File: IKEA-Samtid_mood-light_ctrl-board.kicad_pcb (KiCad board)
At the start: 2 copper layers, 41.3 x 15.5 mm, 15 parts, among them IC1 ATMEGA168PA-M, P1 FTDI, P3.2 B-to-B-1B, P4.2 B-to-B-2B, SW1 ENTER, SW2 MODE, X1 CSTCE16M0V53-R0

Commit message: Being creative...
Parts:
- added DS1: DIODESCH, my_parts:MADW__diode_sub-SMA, F.Cu at (135.1, 95.6)
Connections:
- C1 pad 1: /VCC.B -> /VCC.B2
- IC1 pad 18: /VCC.B -> /VCC.B2
- IC1 pad 30: /RXI -> /RXI.B
- IC1 pad 31: /TXO -> /TXO.B
- IC1 pad 4: /VCC.B -> /VCC.B2
- IC1 pad 6: /VCC.B -> /VCC.B2
- IC1 pad 9: (no net) -> /LEDS.B
- JP1 pad 2: /VCC.B -> /VCC.B2
- P1 pad 3: /VCC.B -> /VCC.B2
- P1 pad 4: /RXI -> /RXI.B
- P1 pad 5: /TXO -> /TXO.B
- P3.2 pad 1: /TXO -> /LEDS.B
- P4.2 pad 1: (no net) -> /RXI.B
- P4.2 pad 3: (no net) -> /TXO.B
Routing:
- net /VCC.B2: track 0.00 -> 40.1 mm, vias 0 -> 3
- net /VCC.B: track 34.8 -> 4.26 mm, vias 3 -> 0
- net /TXO: track 19.4 -> 0.00 mm
- net /TXO.B: track 0.00 -> 18.6 mm
- net /RXI.B: track 0.00 -> 15.8 mm, vias 0 -> 1
- net /LEDS.B: track 0.00 -> 9.26 mm, vias 0 -> 1
- net /RXI: track 4.51 -> 0.00 mm, vias 1 -> 0
- net /MOSI: track 23.1 -> 24.7 mm
- net /XTAL1: track 5.93 -> 6.52 mm
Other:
- board text added: "mood-l. ctrl V0.40.a"
- board text removed: "mood-l. ctrl V0.31.b"

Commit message: 180-d the microMaTch connectors to prevent plugging in old boards.
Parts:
- DS1: value DIODESCH -> SS14L
- turned P3.2 to 116 degrees
- turned P4.2 to 64 degrees
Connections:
- P3.2 pad 1: /LEDS.B -> /GND.B
- P3.2 pad 2: /VCC.B -> /GND.B
- P3.2 pad 3: /GND.B -> /VCC.B
- P3.2 pad 4: /GND.B -> /LEDS.B
- P4.2 pad 1: /RXI.B -> /TXO.B
- P4.2 pad 3: /TXO.B -> /RXI.B
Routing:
- net /TXO.B: track 18.6 -> 17.4 mm
- net /RXI.B: track 15.8 -> 16.8 mm

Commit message: Playing with HC-05 placement.
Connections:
- C2 pad 2: /DTR -> /DTR.B
- P1 pad 6: /DTR -> /DTR.B
- P3.2 pad 2: /GND.B -> /DTR.B
- R2 pad 2: /DTR -> /DTR.B
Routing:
- net /DTR.B: track 0.00 -> 27.9 mm, vias 0 -> 6
- net /DTR: track 6.57 -> 0.00 mm
- net /RXI.B: track 16.8 -> 18.2 mm
- net /ADC2: track 9.76 -> 10.3 mm
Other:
- board text added: "3V!"
- board text removed: "5V!"

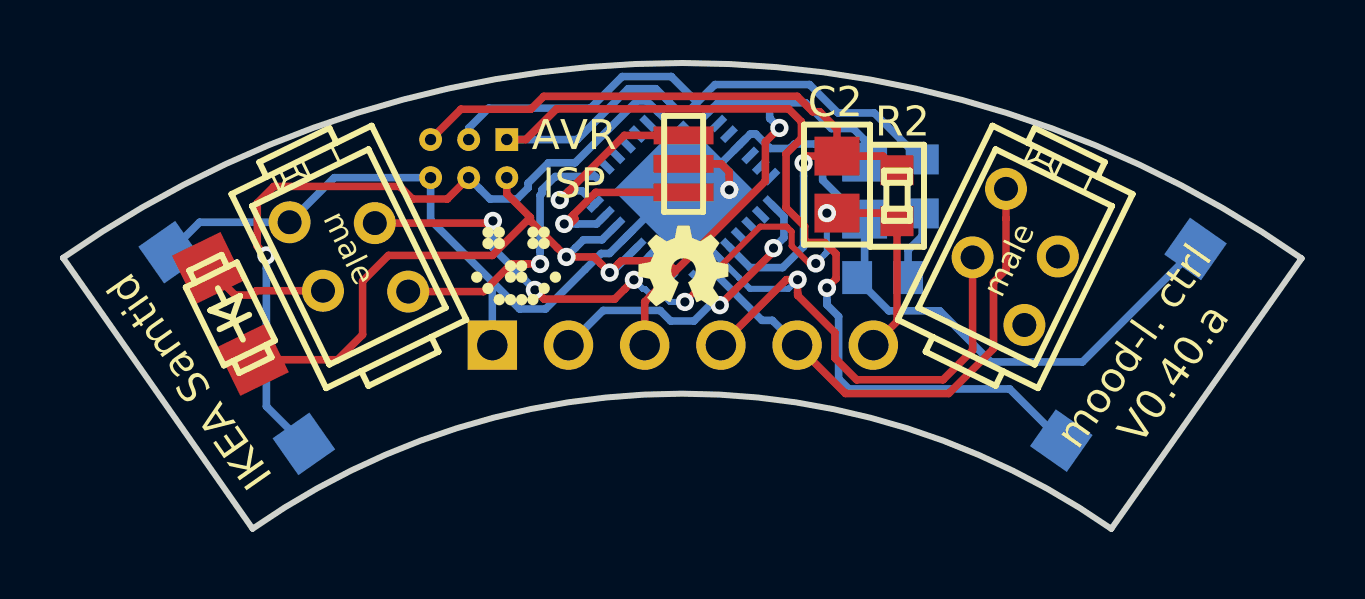
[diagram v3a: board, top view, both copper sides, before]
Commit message: HC-05 tweaks. Forgot about on-board 3.3V regulator.
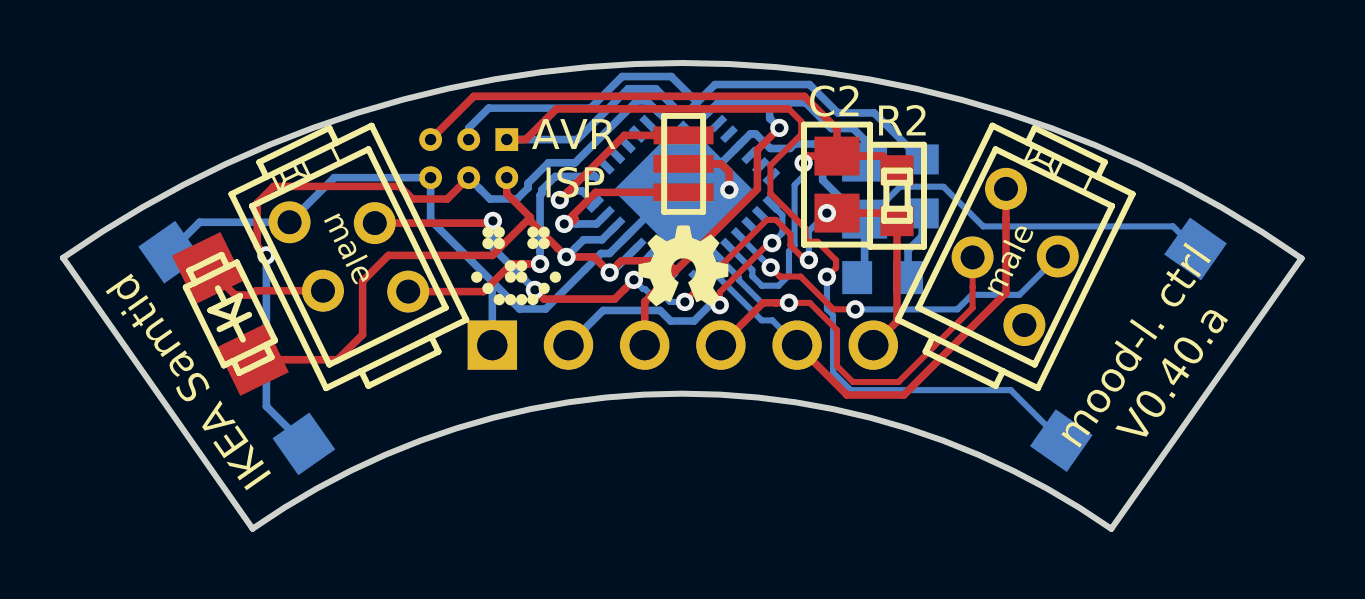
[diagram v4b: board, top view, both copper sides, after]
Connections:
- IC1 pad 28: (no net) -> /KEY.B
- P4.2 pad 2: (no net) -> /KEY.B
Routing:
- net /KEY.B: track 0.00 -> 12.4 mm, vias 0 -> 2
- net /RXI.B: track 18.2 -> 16.5 mm
- net /GND.B: track 55.8 -> 54.2 mm
- net /RST: track 24.8 -> 25.7 mm
- net /TXO.B: track 17.4 -> 16.6 mm

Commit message: Removed 'bleeder' resistor on auto-reset capacitor, replaced with 10k pull-up for reset.
Auto reset works with:

* FTDI cable
* other FTDI-based adapter
* HC-05 Bluetooth module (most of the time)
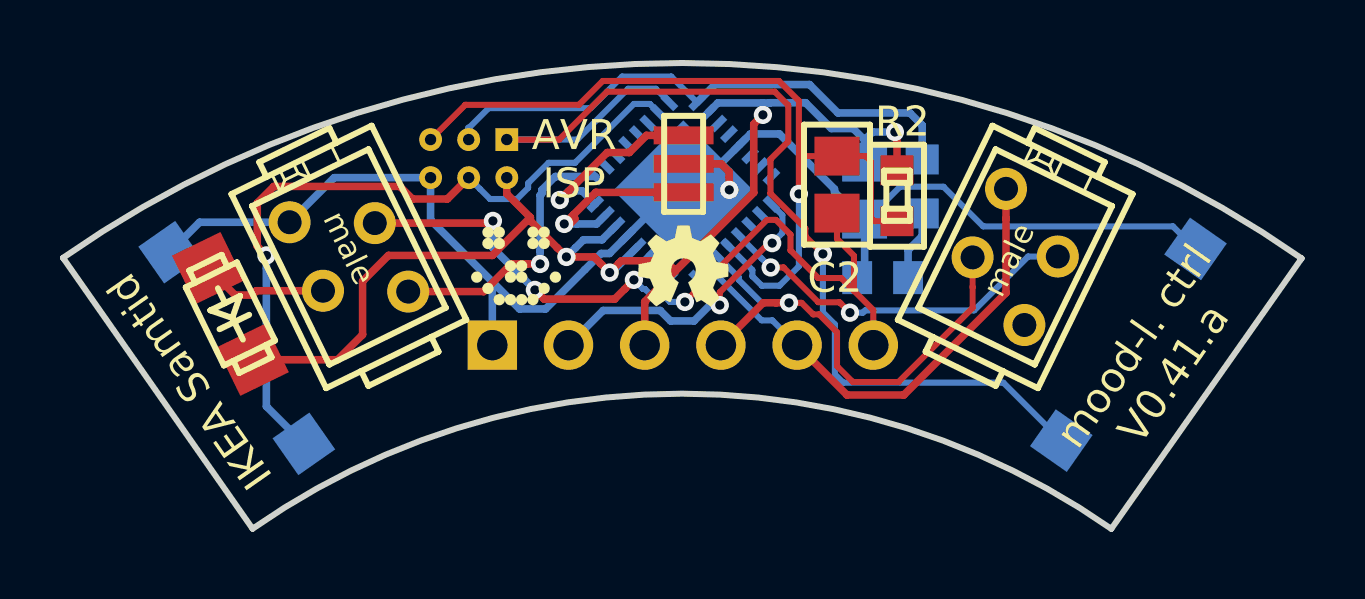
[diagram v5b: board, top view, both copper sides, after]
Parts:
- C2: value 100nF -> 1nF
- R2: value 100k -> 10k
- turned C2 to 90 degrees
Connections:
- C2 pad 1: /RST -> /DTR.B
- C2 pad 2: /DTR.B -> /RST
- R2 pad 1: /RST -> /VCC.B2
- R2 pad 2: /DTR.B -> /RST
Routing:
- net /VCC.B2: track 40.0 -> 42.1 mm, vias 3 -> 4
- net /DTR.B: track 28.0 -> 26.1 mm, vias 6 -> 4
- net /RST: track 25.7 -> 27.6 mm
- net /SCK: track 17.8 -> 18.5 mm
- net /GND.B: track 54.2 -> 53.5 mm
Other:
- board text added: "mood-l. ctrl V0.41.a"
- board text removed: "mood-l. ctrl V0.40.a"

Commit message: Simplifications.
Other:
- board text added: "mood-l. ctrl V0.42.a"
- board text removed: "mood-l. ctrl V0.41.a"
